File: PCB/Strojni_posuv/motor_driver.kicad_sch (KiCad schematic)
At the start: 50 parts, among them IC1 TB6600HG, J3 OUT1, J4 OUT2, Q1 BSS138, Q2 BSS138, Q3 BSS138, Q4 BSS138, Q5 BSS138, Q6 BSS138, Q7 BC847, U3 6N137, U5 6N137, U6 PC817, U7 74HC14

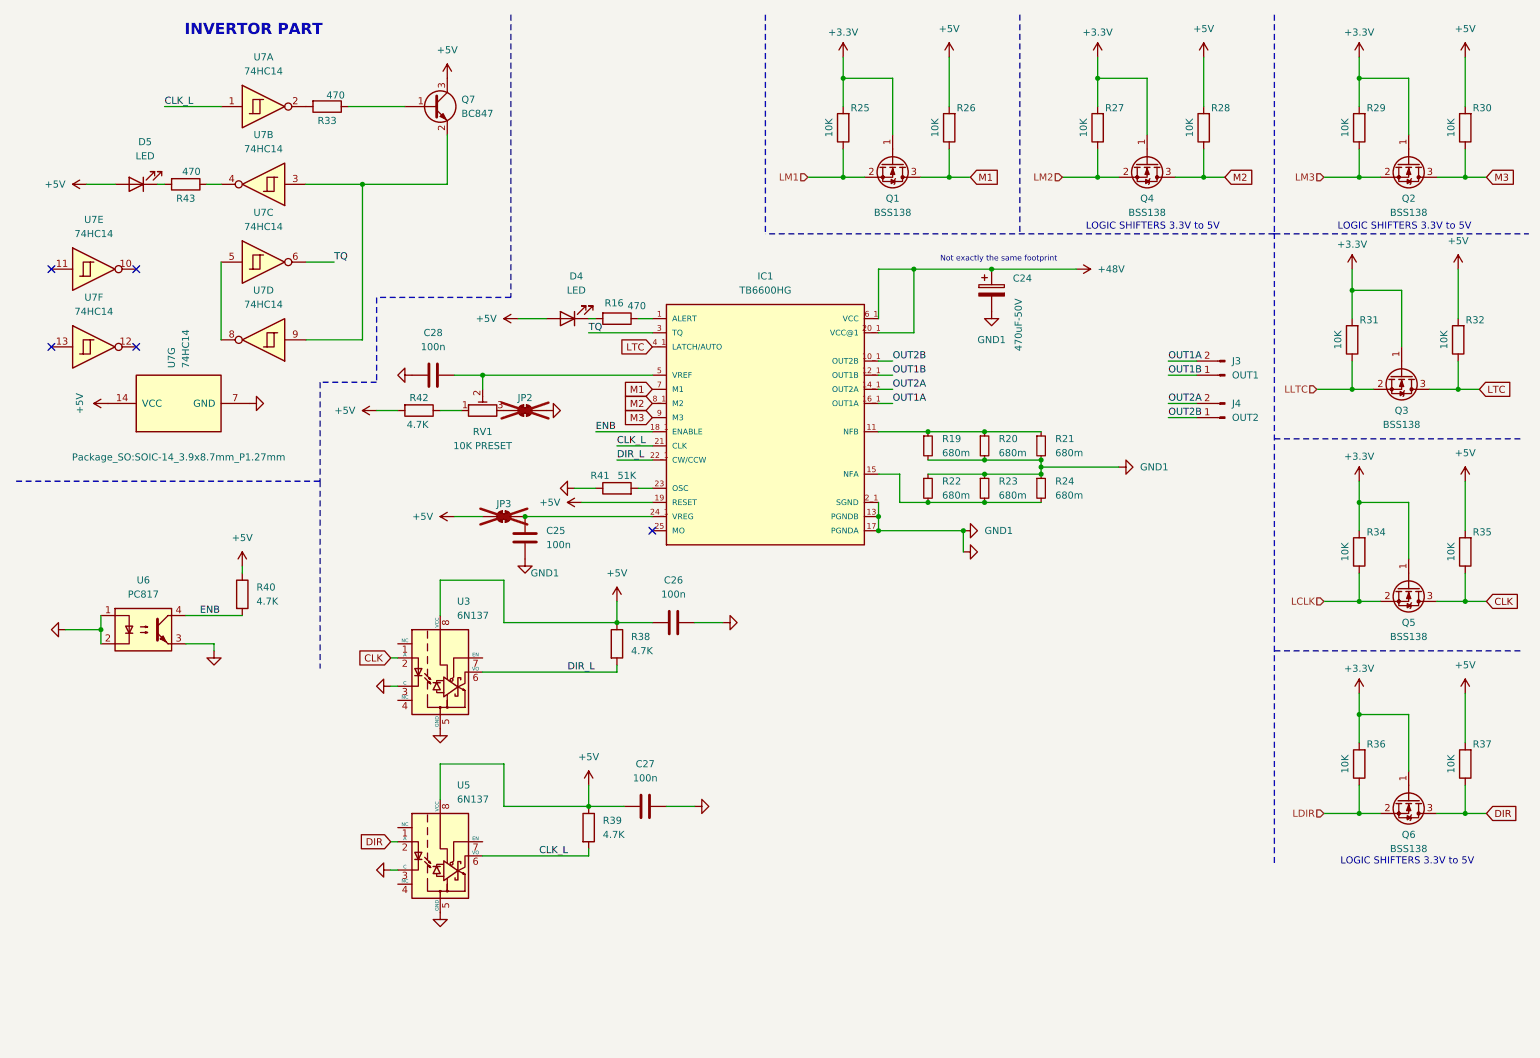
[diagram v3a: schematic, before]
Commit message: New chapter of PCB making #1
the grind continuesmkdir Useful_materials. redundant systems for 5V logic shifting. 2. rotary encoder. 3. new buttons. 4. placement of components (it is not completed)
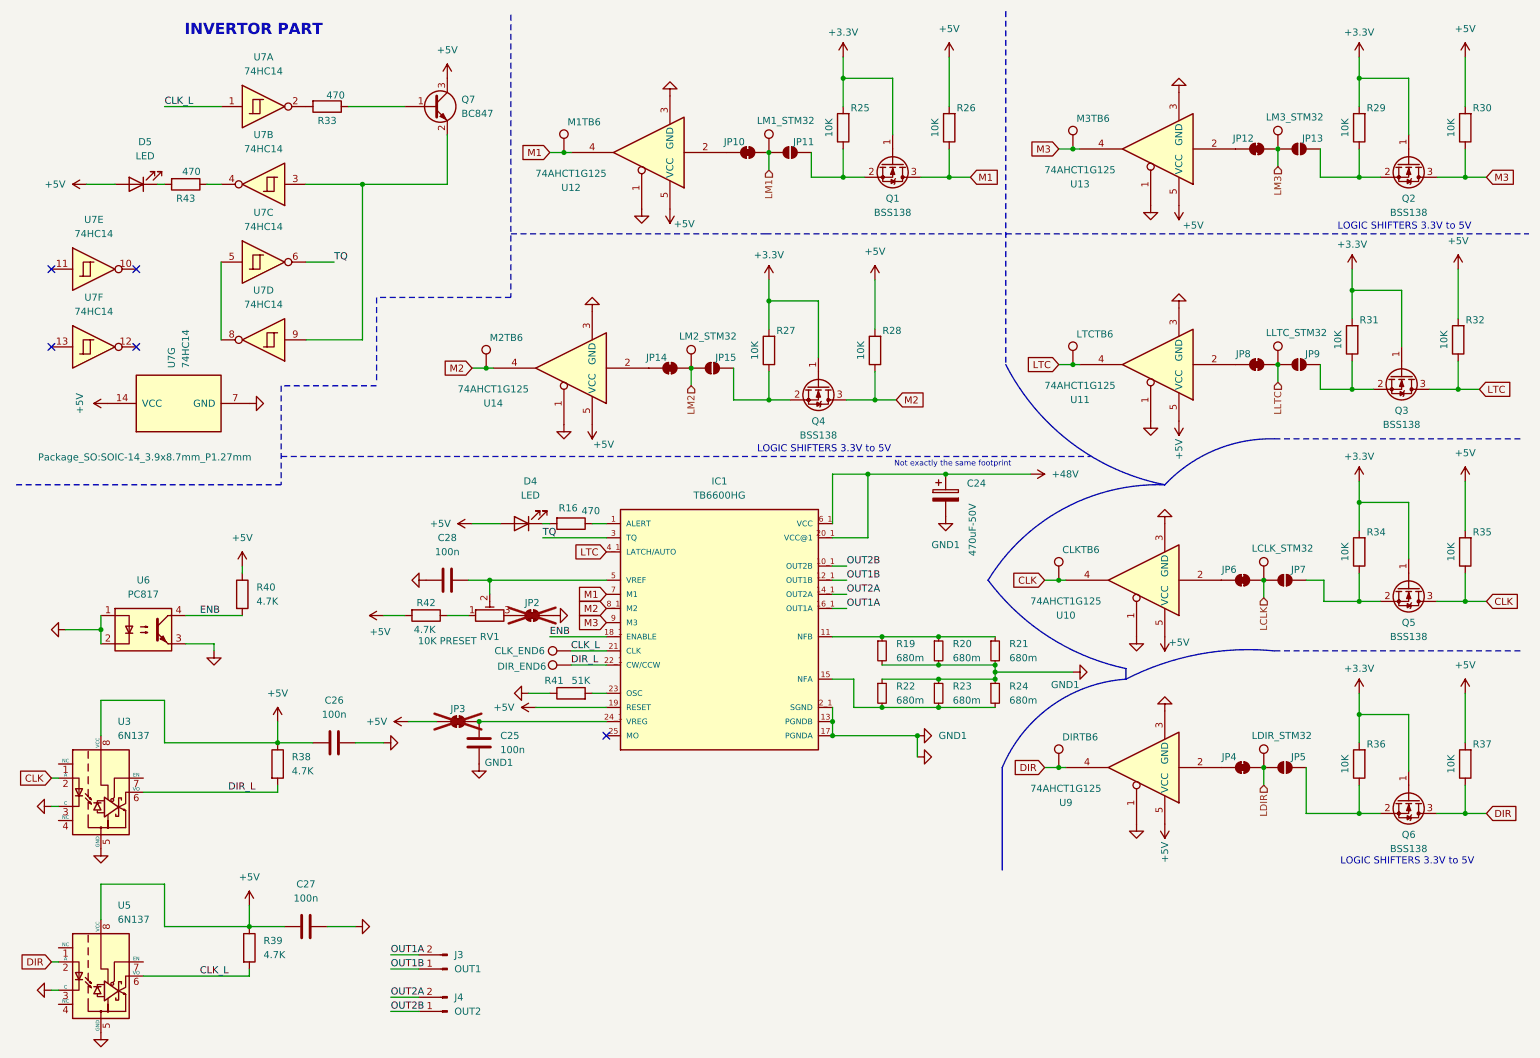
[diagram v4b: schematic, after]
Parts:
- added CLKTB6, CLK_END6, DIRTB6, DIR_END6, LCLK_STM32, LDIR_STM32, LLTC_STM32, LM1_STM32, LM2_STM32, LM3_STM32, LTCTB6, M1TB6, M2TB6, M3TB6: ~, TestPoint:TestPoint_Pad_D1.0mm, symbol Connector:TestPoint
- added JP10, JP12, JP14, JP4, JP6, JP8: SolderJumper_2_Bridged, Jumper:SolderJumper-2_P1.3mm_Bridged_RoundedPad1.0x1.5mm, symbol Jumper:SolderJumper_2_Bridged
- added JP11, JP13, JP15, JP5, JP7, JP9: SolderJumper_2_Open, Jumper:SolderJumper-2_P1.3mm_Open_RoundedPad1.0x1.5mm, symbol Jumper:SolderJumper_2_Open
- added U10, U11, U12, U13, U14, U9: 74AHCT1G125, Package_TO_SOT_SMD:SOT-353_SC-70-5, symbol 74xGxx:74AHCT1G125
- J3, J4: footprint (none) -> Connector_PinSocket_2.54mm:PinSocket_1x02_P2.54mm_Vertical
- RV1: footprint (none) -> Potentiometer_SMD:Potentiometer_Bourns_3314G_Vertical; LSCS (none) -> C780220
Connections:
- net +5V: now also U10.5 (VCC), U11.5 (VCC), U12.5 (VCC), U13.5 (VCC), U14.5 (VCC), U9.5 (VCC)
- net CLK: now also CLKTB6.1, U10.4
- net CLK_L: now also CLK_END6.1
- net DIR: now also DIRTB6.1, U9.4
- net DIR_L: now also DIR_END6.1
- net GND: now also U10.1, U10.3 (GND), U11.1, U11.3 (GND), U12.1, U12.3 (GND), U13.1, U13.3 (GND), U14.1, U14.3 (GND), U9.1, U9.3 (GND)
- net LCLK: now also JP6.2 (B), JP7.1 (A), LCLK_STM32.1; no longer Q5.2 (S), R34.1
- net LDIR: now also JP4.2 (B), JP5.1 (A), LDIR_STM32.1; no longer Q6.2 (S), R36.1
- net LLTC: now also JP8.2 (B), JP9.1 (A), LLTC_STM32.1; no longer Q3.2 (S), R31.1
- net LM1: now also JP10.2 (B), JP11.1 (A), LM1_STM32.1; no longer Q1.2 (S), R25.1
- net LM2: now also JP14.2 (B), JP15.1 (A), LM2_STM32.1; no longer Q4.2 (S), R27.1
- net LM3: now also JP12.2 (B), JP13.1 (A), LM3_STM32.1; no longer Q2.2 (S), R29.1
- net LTC: now also LTCTB6.1, U11.4
- net M1: now also M1TB6.1, U12.4
- net M2: now also M2TB6.1, U14.4
- net M3: now also M3TB6.1, U13.4
- new net: JP5.2 (B), Q6.2 (S), R36.1
- new net: JP9.2 (B), Q3.2 (S), R31.1
- new net: JP7.2 (B), Q5.2 (S), R34.1
- new net: JP15.2 (B), Q4.2 (S), R27.1
- new net: JP4.1 (A), U9.2
- new net: JP11.2 (B), Q1.2 (S), R25.1
- new net: JP14.1 (A), U14.2
- new net: JP13.2 (B), Q2.2 (S), R29.1
- new net: JP8.1 (A), U11.2
- new net: JP10.1 (A), U12.2
- new net: JP6.1 (A), U10.2
- new net: JP12.1 (A), U13.2
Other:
- moved on the sheet: C24, C25, C26, C27, C28, D4, IC1, J3, J4, JP2, JP3, Q4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

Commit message: Revision 0
The PCB is done
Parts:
- D4, D5: LCSC (none) -> C84266
- RV1: LCSC (none) -> C780220; LSCS C780220 -> (none)
- U7: Field5 C5605 -> (none); LCSC (none) -> C5605

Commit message: Revision 0 - final
I send this files to JLCPCB
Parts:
- RV1: footprint Potentiometer_SMD:Potentiometer_Bourns_3314G_Vertical -> Potentiometer_SMD:Potentiometer_Bourns_TC33X_Vertical; LCSC C780220 -> C719176
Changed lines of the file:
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@@
 			)
 		)
-		(property "Footprint" "Potentiometer_SMD:Potentiometer_Bourns_3314G_Vertical"
+		(property "Footprint" "Potentiometer_SMD:Potentiometer_Bourns_TC33X_Vertical"
 			(at 97.79 120.65 0)
 			(effects
@@
 			)
 		)
-		(property "LCSC" "C780220"
+		(property "LCSC" "C719176"
 			(at 97.79 120.65 90)
 			(effects

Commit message: Last version before making new revision
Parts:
- removed R40: 4.7K, Resistor_SMD:R_0603_1608Metric, symbol Device:R
- removed U6: PC817, Package_DIP:DIP-4_W8.89mm_SMDSocket_LongPads, symbol Isolator:PC817
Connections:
- net ENB is gone; now on net +5V: IC1.18_1 (ENABLE)
- net CLK_L: now also R38.2, U3.6 (VO); no longer R39.2, U5.6 (VO)
- net DIR_L: now also R39.2, U5.6 (VO); no longer R38.2, U3.6 (VO)

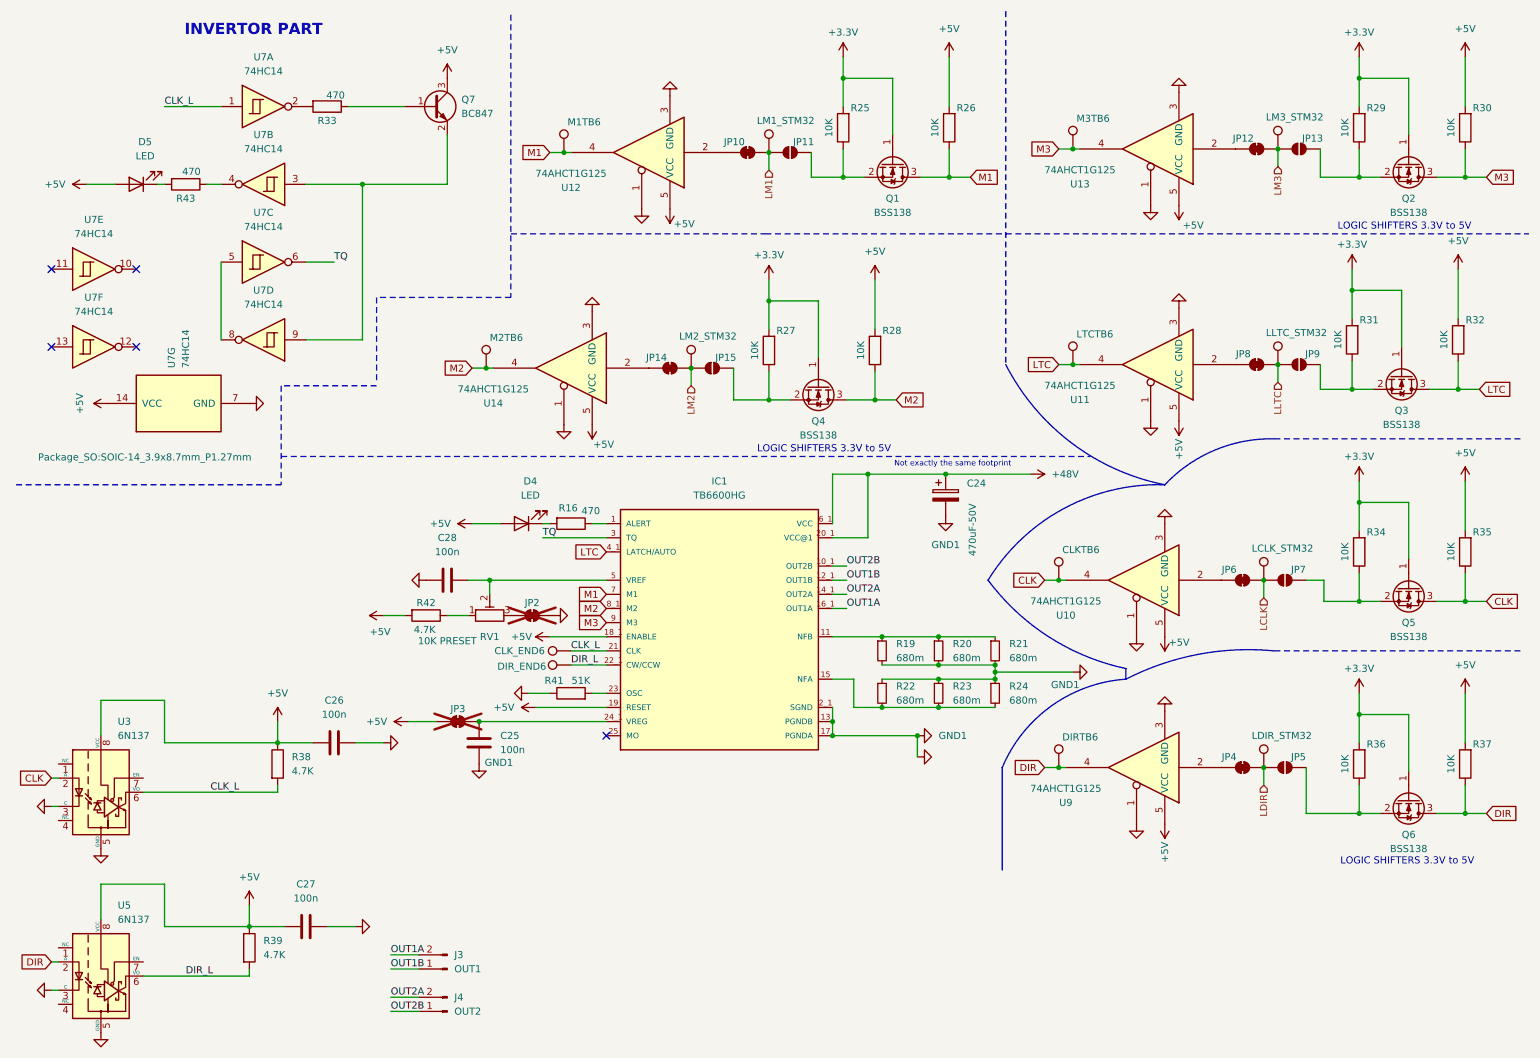
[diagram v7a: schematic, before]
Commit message: Starting new Revision 1
addressing some problems and mistakes
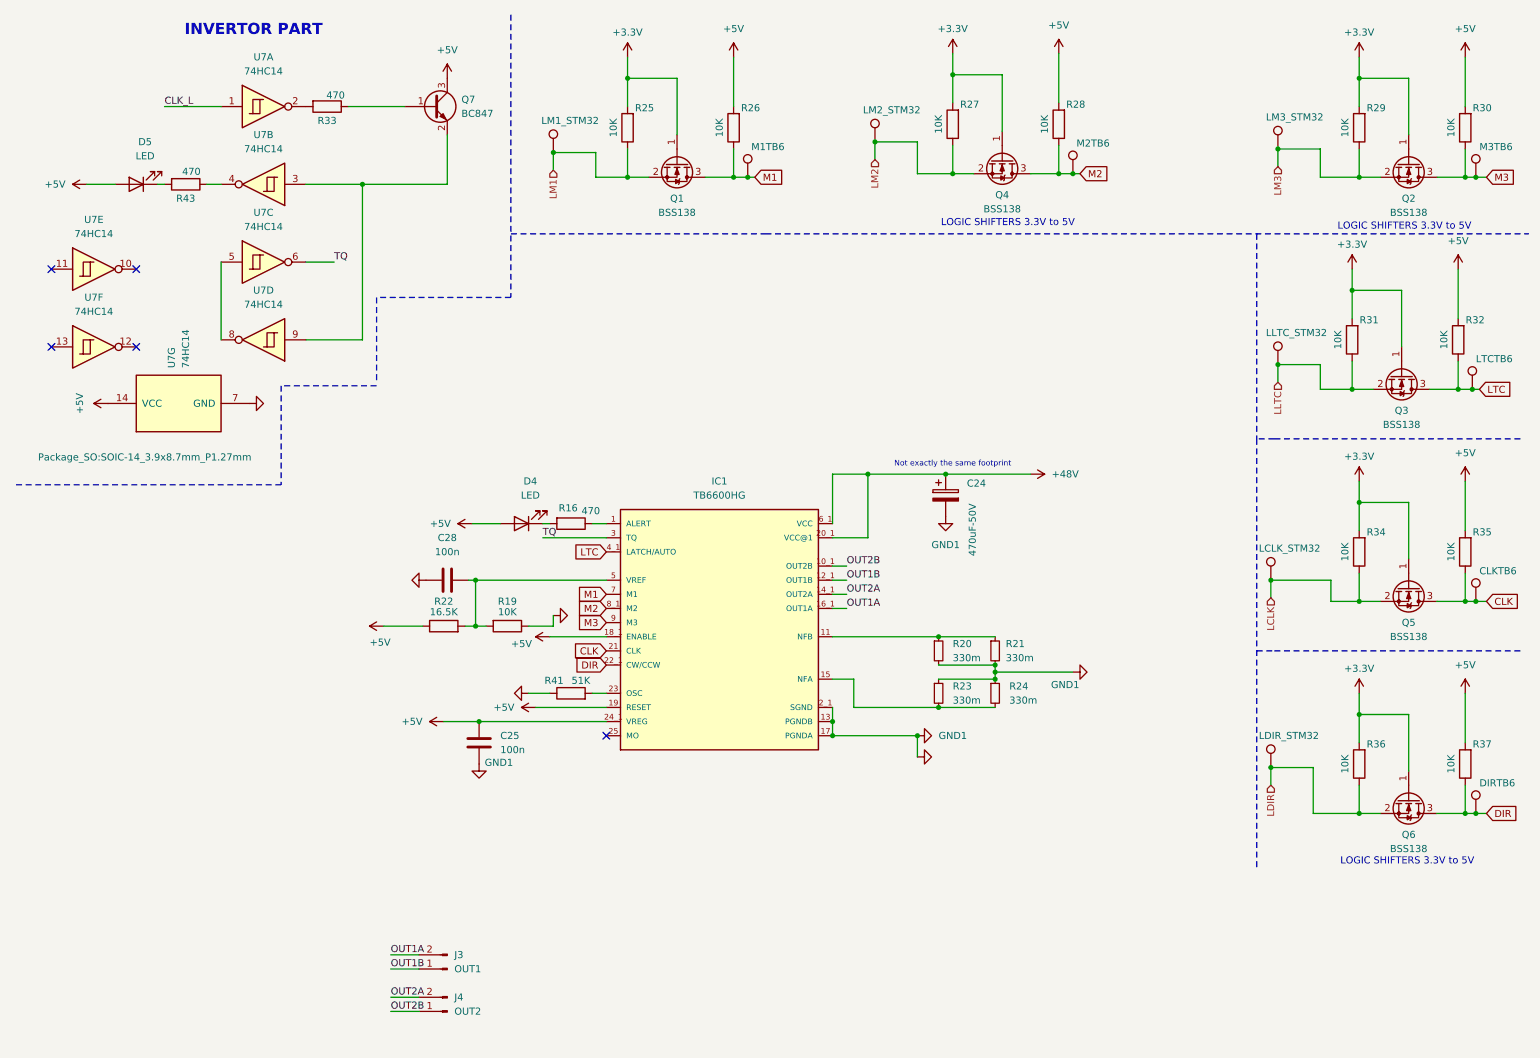
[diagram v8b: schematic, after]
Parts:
- removed C26, C27: 100n, Capacitor_SMD:C_0603_1608Metric, symbol Device:C
- removed CLK_END6, DIR_END6: ~, TestPoint:TestPoint_Pad_D1.0mm, symbol Connector:TestPoint
- removed JP10, JP12, JP14, JP2, JP3, JP4, JP6, JP8: SolderJumper_2_Bridged, Jumper:SolderJumper-2_P1.3mm_Bridged_RoundedPad1.0x1.5mm, symbol Jumper:SolderJumper_2_Bridged
- removed JP11, JP13, JP15, JP5, JP7, JP9: SolderJumper_2_Open, Jumper:SolderJumper-2_P1.3mm_Open_RoundedPad1.0x1.5mm, symbol Jumper:SolderJumper_2_Open
- removed R19, R22: 680m, Resistor_SMD:R_1206_3216Metric, symbol Device:R_Small
- removed R38, R39, R42: 4.7K, Resistor_SMD:R_0603_1608Metric, symbol Device:R
- removed RV1: 10K PRESET, Potentiometer_SMD:Potentiometer_Bourns_TC33X_Vertical, symbol Device:R_Potentiometer_Trim
- removed U10, U11, U12, U13, U14, U9: 74AHCT1G125, Package_TO_SOT_SMD:SOT-353_SC-70-5, symbol 74xGxx:74AHCT1G125
- removed U3, U5: 6N137, Package_SO:SOP-8_6.605x9.655mm_P2.54mm, symbol Isolator:6N137
- added R19: 10K, Resistor_SMD:R_0805_2012Metric, symbol Device:R
- added R22: 16.5K, Resistor_SMD:R_0805_2012Metric, symbol Device:R
- R16, R25, R26, R27, R28, R29, R30, R31, R32, R33, R34, R35, R36, R37, R41, R43: footprint Resistor_SMD:R_0603_1608Metric -> Resistor_SMD:R_0805_2012Metric
- R20, R21, R23, R24: value 680m -> 330m; footprint Resistor_SMD:R_1206_3216Metric -> Resistor_THT:R_Axial_DIN0922_L20.0mm_D9.0mm_P30.48mm_Horizontal
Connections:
- net DIR_L is gone; now on net DIR: IC1.22_1 (CW/CCW)
- net +5V: now also C25.1, IC1.24_1 (VREG), R22.1
- net CLK: now also IC1.21 (CLK)
- net CLK_L: no longer IC1.21 (CLK)
- net GND: now also R19.1
- net LCLK: now also Q5.2 (S), R34.1
- net LDIR: now also Q6.2 (S), R36.1
- net LLTC: now also Q3.2 (S), R31.1
- net LM1: now also Q1.2 (S), R25.1
- net LM2: now also Q4.2 (S), R27.1
- net LM3: now also Q2.2 (S), R29.1
- net at C28.2, IC1.5 (VREF): now also R19.2, R22.2
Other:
- moved on the sheet: CLKTB6, DIRTB6, LCLK_STM32, LDIR_STM32, LM1_STM32, LM2_STM32, LTCTB6, M1TB6, M2TB6, M3TB6, Q1, Q4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
